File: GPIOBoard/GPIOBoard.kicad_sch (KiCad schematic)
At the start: 52 parts, among them J1 GPIO1, J12 CAN, J2 GPIO2, J3 GPIO3, J4 GPIO4, J5 GPIO5, J6 GPIO6, J7 GPIO7, J8 GPIO8, J9 IMU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

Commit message: GPIO Board ver1.1
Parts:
- removed SW3: CAN_R, Anan-Robo_Footprint_Library:SSSS213202, symbol Switch:SW_SPDT
- removed U2: LM1117GS, Package_TO_SOT_SMD:SOT-223-3_TabPin2, symbol Anan-Robo_Symbol_Library:LM1117GS
- added D17: CAN_R, LED_SMD:LED_0603_1608Metric, symbol Device:LED
- added R27: 420, Resistor_SMD:R_0603_1608Metric, symbol Device:R
- added R28: 100, Resistor_SMD:R_0603_1608Metric, symbol Device:R
- added R29: 600, Resistor_SMD:R_0603_1608Metric, symbol Device:R
- added R30: 300, Resistor_SMD:R_0603_1608Metric, symbol Device:R
- added SW3: CAN_R, Anan-Robo_Footprint_Library:SLW, symbol Switch:SW_DPDT_x2
- added U2: TLV1117-33, Package_TO_SOT_SMD:SOT-223-3_TabPin2, symbol Regulator_Linear:TLV1117-33
- added U5: LED_GRB, LED_SMD:LED_ROHM_SMLVN6, symbol Anan-Robo_Symbol_Library:LED_GRB
- C1: value 10u -> 4.7u; Name GRM188R60J476ME01D -> GRM188R60J226MEA0D; Price 56 -> 30; URL https://www.digikey.jp/ja/products/detail/murata-electronics/GRM188R60J476ME01D/13996874 -> https://www.digikey.jp/ja/products/detail/murata-electronics/GRM188R60J226MEA0D/4280542
- C2: value 10u -> 4.7u; Name CL10A226MP8NUNE -> GRM188R60G106ME47D; Price 16 -> 19; URL https://www.digikey.jp/ja/products/detail/samsung-electro-m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 -> https://www.digikey.jp/ja/products/detail/murata-electronic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
- D1, D2, D3, D4, D5, D6, D7, D8: Name SMLEN3BC8TT86 -> SMLD12BN1WT86; Price 92 -> 48; URL https://www.digikey.jp/ja/products/detail/rohm-semiconductor/SMLEN3BC8TT86/15762415 -> https://www.digikey.jp/ja/products/detail/rohm-semiconductor/SMLD12BN1WT86/9826162
- D10, D9: Name SML-E12P8WT86 -> SML-D14MWT86A; Price 39 -> 53; URL https://www.digikey.jp/ja/products/detail/rohm-semiconductor/SML-E12P8WT86/1641804 -> https://www.digikey.jp/ja/products/detail/rohm-semiconductor/SML-D14MWT86A/9448204
- D11: Name SML-E12DWT86 -> SML-D12D8WT86; Price 58 -> 30; URL https://www.digikey.jp/ja/products/detail/rohm-semiconductor/SML-E12DWT86/2337250 -> https://www.digikey.jp/ja/products/detail/rohm-semiconductor/SML-D12D8WT86/1641796
- D16: footprint Diode_SMD:D_SOD-123 -> Diode_SMD:Nexperia_CFP3_SOD-123W; Name RB160M-30TR -> PMEG3010ER,115; Price 15 -> 30; URL https://akizukidenshi.com/catalog/g/g101398/ -> https://www.digikey.jp/ja/products/detail/nexperia-usa-inc/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
- H1, H2, H3, H4: Name (none) -> -; Price (none) -> -; URL (none) -> -
- J1, J2, J3, J4, J5, J6, J7, J8: URL (none) -> https://www.digikey.jp/ja/products/detail/jst-sales-america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
- R1, R2, R3, R4, R5, R6, R7, R8: Name ESR03EZPF82R0 -> ESR03EZPJ820; Price 23 -> 22; URL https://www.digikey.jp/ja/products/detail/rohm-semiconductor/ESR03EZPF82R0/4007286 -> https://www.digikey.jp/ja/products/detail/rohm-semiconductor/ESR03EZPJ820/4051294
- R10, R11, R12, R13, R14, R15, R16, R9: Name ESR03EZPF3300 -> ESR03EZPJ301; Price 23 -> 22; URL https://www.digikey.jp/ja/products/detail/rohm-semiconductor/ESR03EZPF3300/4007217 -> https://www.digikey.jp/ja/products/detail/rohm-semiconductor/ESR03EZPJ301/1762729
- R17, R18: value 55 -> 96; Name ESR03EZPF60R4 -> ESR03EZPJ101; Price 23 -> 22; URL https://www.digikey.jp/ja/products/detail/rohm-semiconductor/ESR03EZPF60R4/20486478 -> https://www.digikey.jp/ja/products/detail/rohm-semiconductor/ESR03EZPJ101/1983452
- R19: value 150 -> 430; Name ESR03EZPF1500 -> ESR03EZPJ431; Price 23 -> 22; URL https://www.digikey.jp/ja/products/detail/rohm-semiconductor/ESR03EZPF1500/4007164 -> https://www.digikey.jp/ja/products/detail/rohm-semiconductor/ESR03EZPJ431/4051257?s=N4IgjCBcoCwGxVAYygMwIYBsDOBTANCAPZQDaIA7ABwAMATCALqEAOALlCAMpsBOAlgDsA5iAC%2BhMAE4qUxCBSQMOAsTIgaTCSDo0qAVnmLleQiUjkYAZhoACAPIALALbYmrDpBABVQfzb2qACyuOjYAK68uOKEALRy0ApQfOGq5uQQjNqxDImKKWnqhllxEHloWKZqFiBU8FpxMEYVKmbqVnUUCFnaueSAgwyAwwyA6wyArUaA6UZaQA
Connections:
- net +3.3V: now also U2.2 (VO)
- net +5V: now also D17.2 (A), U2.3 (VI)
- net CAN/CAN_L: now also SW3.1 (A)
- net GNDD: now also SW3.4 (A), U2.1 (GND), U5.4, U5.5, U5.6
- net at R25.2: now also SW3.2 (B)
- new net: D17.1 (K), R27.1
- new net: R27.2, SW3.5 (B)
- new net: R28.1, U5.1
- new net: R29.1, U5.2
- new net: R30.1, U5.3
- new net MCU/LED_B: R28.2
- new net MCU/LED_G: R30.2
- new net MCU/LED_R: R29.2
- no-connect marks 1 -> 2
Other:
- sheet MCU ports: added LED_B, LED_G, LED_R; removed none
- note added: "Vcc = 3.3V Vf = 2.1V, If = 12.5mA (3.3-2.1) / 0.0125 = 96Ω"
- note added: "Vcc = 5.0V Vf = 2.2V, If = 6.5mA (5.0-2.2) / 0.0065 = 430Ω"
- note added: "Vcc = 5V Vf = 2.9V, If = 5mA (5 - 2.9) / 0.005 = 420Ω"
- note removed: "Vcc = 3.3V Vf = 2.2V, If = 20mA (3.3-2.2) / 0.02 = 55Ω"
- note removed: "Vcc = 5.0V Vf = 2.0V, If = 20mA (5.0-2.0) / 0.02 = 150Ω"
- company: (none) -> 阿南高専ロボット研究部
- title: (none) -> GPIO Board
- moved on the sheet: H1

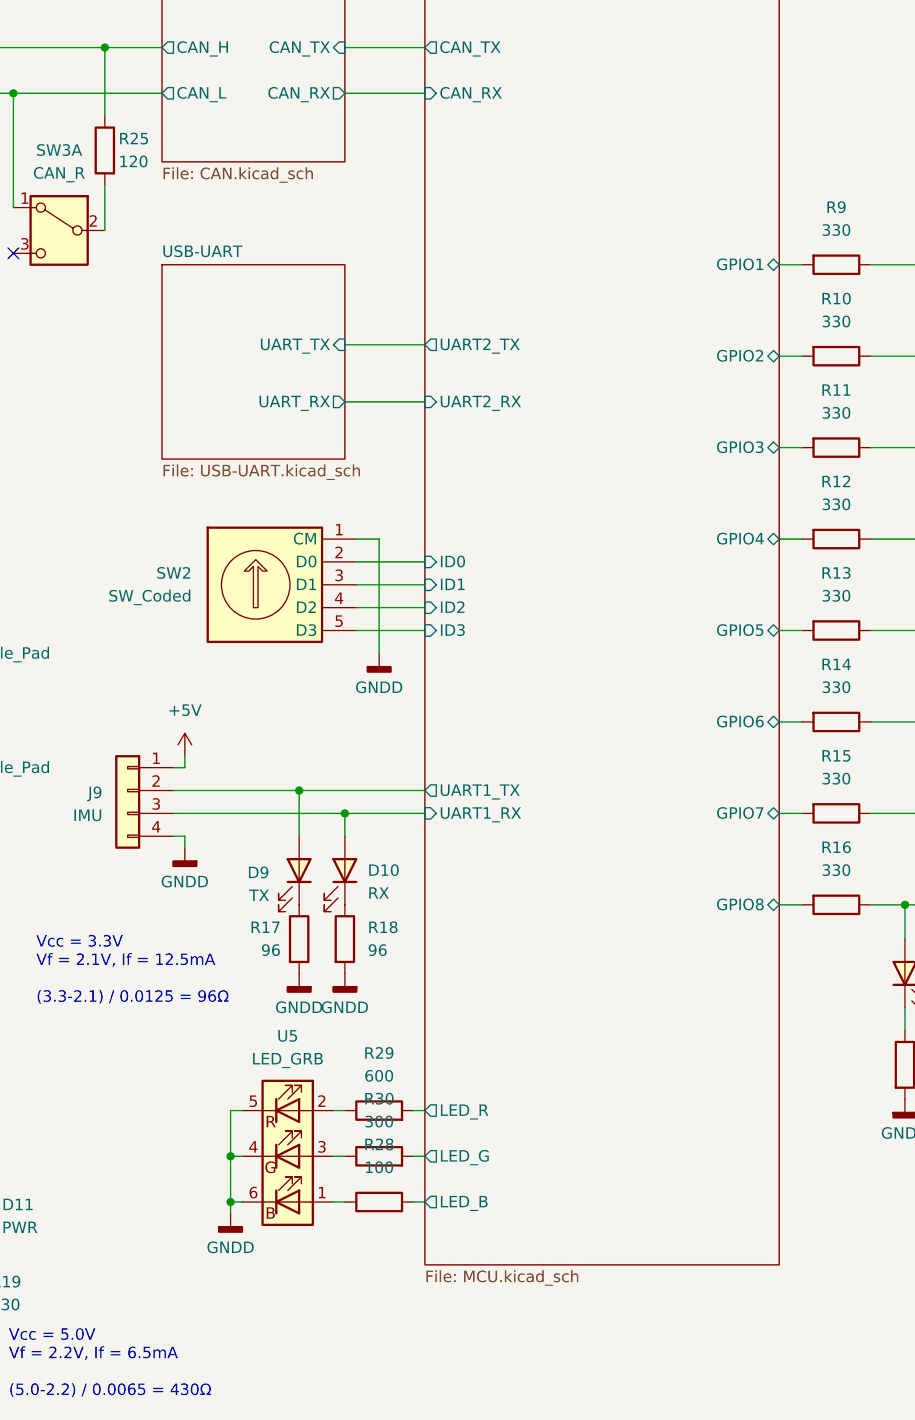
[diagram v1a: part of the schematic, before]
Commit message: GPIO Board ver1.2
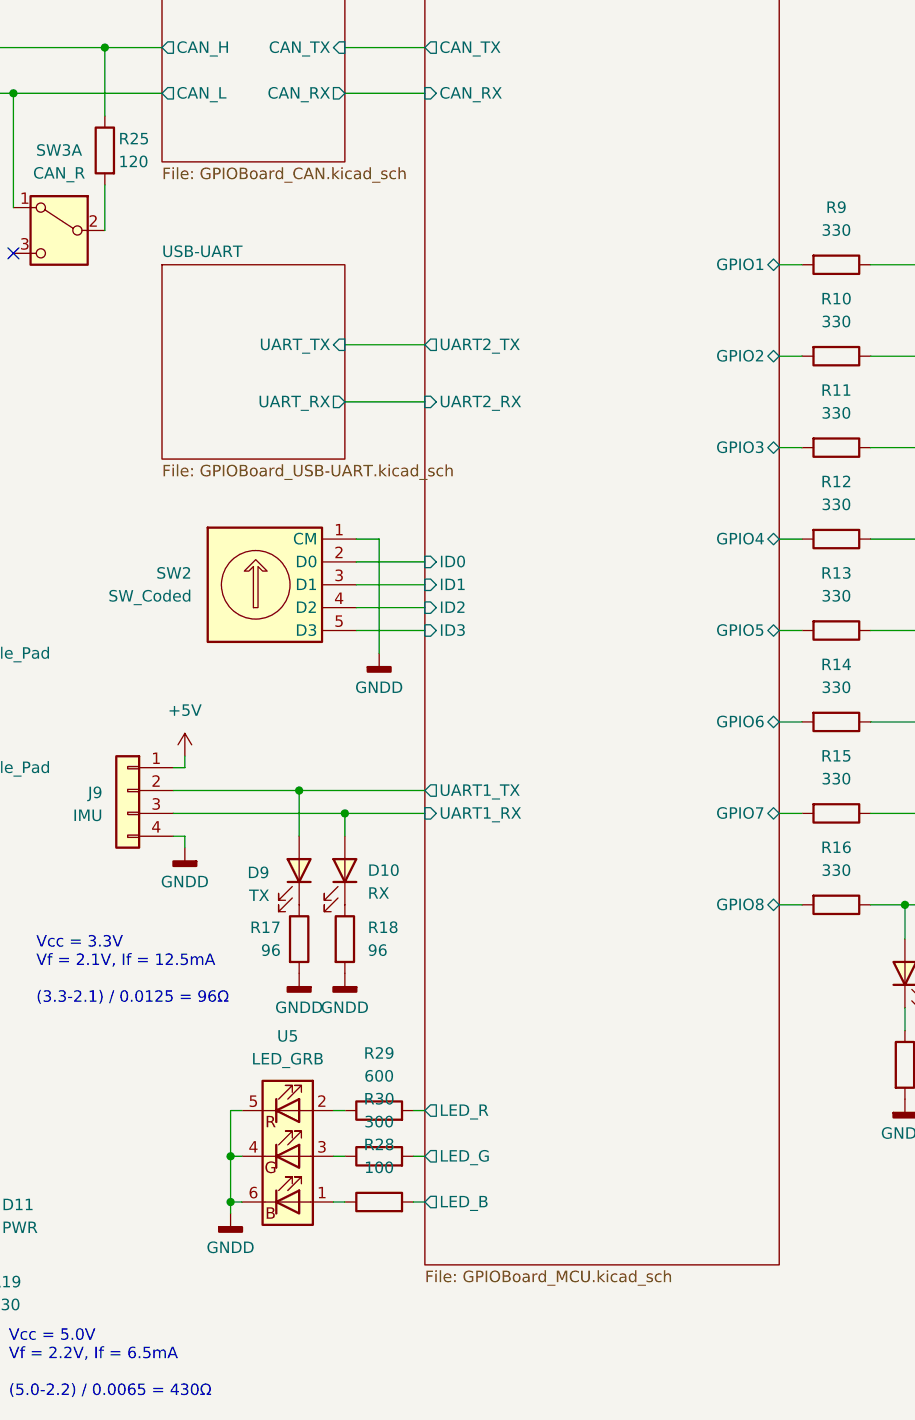
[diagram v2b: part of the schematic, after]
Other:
- sheet CAN: file CAN.kicad_sch -> GPIOBoard_CAN.kicad_sch
- sheet MCU: file MCU.kicad_sch -> GPIOBoard_MCU.kicad_sch
- sheet USB-UART: file USB-UART.kicad_sch -> GPIOBoard_USB-UART.kicad_sch
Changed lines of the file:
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@@
 	(title_block
 		(title "GPIO Board")
-		(date "2025-04-03")
-		(rev "ver1.1")
+		(date "2025-07-01")
+		(rev "ver1.2")
 		(company "阿南高専ロボット研究部")
 	)
@@
 			)
 		)
-		(property "Sheetfile" "USB-UART.kicad_sch"
+		(property "Sheetfile" "GPIOBoard_USB-UART.kicad_sch"
 			(at 85.09 88.2146 0)
 			(effects
@@
 			)
 		)
-		(property "Sheetfile" "MCU.kicad_sch"
+		(property "Sheetfile" "GPIOBoard_MCU.kicad_sch"
 			(at 114.3 177.7496 0)
 			(effects
@@
 			)
 		)
-		(property "Sheetfile" "CAN.kicad_sch"
+		(property "Sheetfile" "GPIOBoard_CAN.kicad_sch"
 			(at 85.09 55.1946 0)
 			(effects
